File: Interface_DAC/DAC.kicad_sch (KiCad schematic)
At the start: 14 parts, among them U5 PCM1794A

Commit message: Footprint Arrangement
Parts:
- C43, C45, C47, C50: footprint (none) -> Capacitor_Tantalum_SMD:CP_EIA-2012-12_Kemet-R
- C44, C46, C48: footprint (none) -> Capacitor_SMD:C_0402_1005Metric
- C49: footprint (none) -> Capacitor_Tantalum_SMD:CP_EIA-3216-18_Kemet-A
- R11, R12, R4, R5, R8: footprint (none) -> Resistor_SMD:R_0402_1005Metric
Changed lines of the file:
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@@
 			)
 		)
-		(property "Footprint" ""
+		(property "Footprint" "Resistor_SMD:R_0402_1005Metric"
 			(at 69.85 112.268 90)
 			(effects
@@
 			)
 		)
-		(property "Footprint" ""
+		(property "Footprint" "Capacitor_Tantalum_SMD:CP_EIA-2012-12_Kemet-R"
 			(at 89.8652 69.85 0)
 			(effects
@@
 			)
 		)
-		(property "Footprint" ""
+		(property "Footprint" "Resistor_SMD:R_0402_1005Metric"
 			(at 49.53 117.348 90)
 			(effects
@@
 			)
 		)
-		(property "Footprint" ""
+		(property "Footprint" "Resistor_SMD:R_0402_1005Metric"
 			(at 59.69 114.808 90)
 			(effects
@@
 			)
 		)
-		(property "Footprint" ""
+		(property "Footprint" "Capacitor_Tantalum_SMD:CP_EIA-2012-12_Kemet-R"
 			(at 115.2652 62.23 0)
 			(effects
@@
 			)
 		)
-		(property "Footprint" ""
+		(property "Footprint" "Capacitor_SMD:C_0402_1005Metric"
 			(at 125.4252 62.23 0)
 			(effects
@@
 			)
 		)
-		(property "Footprint" ""
+		(property "Footprint" "Resistor_SMD:R_0402_1005Metric"
 			(at 80.01 109.728 90)
 			(effects
@@
 			)
 		)
-		(property "Footprint" ""
+		(property "Footprint" "Capacitor_Tantalum_SMD:CP_EIA-2012-12_Kemet-R"
 			(at 115.2652 85.09 0)
 			(effects
@@
 			)
 		)
-		(property "Footprint" ""
+		(property "Footprint" "Capacitor_Tantalum_SMD:CP_EIA-3216-18_Kemet-A"
 			(at 127.9652 105.41 0)
 			(effects
@@
 			)
 		)
-		(property "Footprint" ""
+		(property "Footprint" "Resistor_SMD:R_0402_1005Metric"
 			(at 128.27 140.208 90)
 			(effects
@@
 			)
 		)
-		(property "Footprint" ""
+		(property "Footprint" "Capacitor_SMD:C_0402_1005Metric"
 			(at 89.8652 90.17 0)
 			(effects
@@
 			)
 		)
-		(property "Footprint" ""
+		(property "Footprint" "Capacitor_SMD:C_0402_1005Metric"
 			(at 125.4252 85.09 0)
 			(effects
@@
 			)
 		)
-		(property "Footprint" ""
+		(property "Footprint" "Capacitor_Tantalum_SMD:CP_EIA-2012-12_Kemet-R"
 			(at 79.7052 90.17 0)
 			(effects

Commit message: Schematic Tinkering and PCB Layout
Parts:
- added C48: 10u, Capacitor_SMD:C_0402_1005Metric, symbol Device:C
- added R6: 47k, Resistor_SMD:R_0402_1005Metric, symbol Device:R
- C40: renamed from C45; footprint Capacitor_Tantalum_SMD:CP_EIA-2012-12_Kemet-R -> Capacitor_SMD:C_0402_1005Metric; symbol Device:C_Polarized -> Device:C
- C42: renamed from C50; footprint Capacitor_Tantalum_SMD:CP_EIA-2012-12_Kemet-R -> Capacitor_SMD:C_0402_1005Metric; symbol Device:C_Polarized -> Device:C
- C43: footprint Capacitor_Tantalum_SMD:CP_EIA-2012-12_Kemet-R -> Capacitor_SMD:C_0402_1005Metric; symbol Device:C_Polarized -> Device:C
- C45: renamed from C47; footprint Capacitor_Tantalum_SMD:CP_EIA-2012-12_Kemet-R -> Capacitor_SMD:C_0402_1005Metric; symbol Device:C_Polarized -> Device:C
- C47: renamed from C49; value 47u -> 10u; footprint Capacitor_Tantalum_SMD:CP_EIA-3216-18_Kemet-A -> Capacitor_SMD:C_0402_1005Metric; symbol Device:C_Polarized -> Device:C
- renumbered C46 to C41, C48 to C46, R5 to R2, R8 to R3, R11 to R4, R12 to R5, R4 to R7, U5 to U4
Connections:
- net +3.3V: now also R6.1
- net GND: now also U4.1 (MONO), U4.10 (MUTE), U4.11 (FMT0), U4.12 (FMT1), U4.2 (CHSL), U4.3 (DEM)
- net VBUS: now also C48.1
- net at C47.2, U4.22 (VCOML): no longer U4.21 (VCOMR)
- net at U4.14 (~{RST}): now also R6.2
- net SCK renamed I2S_SCK
- new net: C48.2, U4.21 (VCOMR)

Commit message: Schematic Tinkering and PCB Layout
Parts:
- added C40, C50, C53, C56: 4.7n, Capacitor_SMD:C_0402_1005Metric, symbol Device:C
- added C43, C49, C54, C55: 10n, Capacitor_SMD:C_0402_1005Metric, symbol Device:C
- added R13, R20, R3, R8: 820, Resistor_SMD:R_0402_1005Metric, symbol Device:R
- added R14, R19, R4, R7: 240, Resistor_SMD:R_0402_1005Metric, symbol Device:R
- added R17, R18, R5, R6: 510, Resistor_SMD:R_0402_1005Metric, symbol Device:R
- added U4, U6: OPA1612AxD, Package_SON:WSON-8-1EP_3x3mm_P0.5mm_EP1.2x2mm_ThermalVias, symbol Amplifier_Operational:OPA1612AxD
- added U5: OPA1612AxD, Package_SO:SOIC-8_3.9x4.9mm_P1.27mm, symbol Amplifier_Operational:OPA1612AxD
- renumbered C40 to C41, C41 to C42, C42 to C44, C43 to C45, C44 to C46, C45 to C47, C46 to C48, C47 to C51, C48 to C52, R3 to R10, R4 to R11, R5 to R12, R6 to R15, R7 to R16, R2 to R9, U4 to U7
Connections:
- net GND: now also C49.2, C55.2, R19.2, R7.2, U4.3 (+), U4.5 (+), U6.3 (+), U6.5 (+)
- net IOUTRP: now reaches U7.17 (IOUTR+)
- net IOUTRP: now also C53.1, R13.1, U6.6 (-)
- net IOUTRN: now reaches U7.18 (IOUTR-)
- net IOUTRN: now also C56.1, R20.1, U6.2 (-)
- net IOUTLP: now reaches U7.25 (IOUTL+)
- net IOUTLP: now also C40.1, R3.1, U4.6 (-)
- net IOUTLN: now reaches U7.26 (IOUTL-)
- net IOUTLN: now also C50.1, R8.1, U4.2 (-)
- new net: C53.2, R13.2, R17.1, U6.7
- new net: C54.1, R14.1, R17.2, U5.6 (-)
- new net: C50.2, R6.1, R8.2, U4.1
- new net: C56.2, R18.1, R20.2, U6.1
- new net: C55.1, R18.2, R19.1, U5.5 (+)
- new net: C43.1, R4.1, R5.2, U5.2 (-)
- new net: C49.1, R6.2, R7.1, U5.3 (+)
- new net: C40.2, R3.2, R5.1, U4.7
- new net +9VA: U4.8 (V+), U5.8 (V+), U6.8 (V+)
- new net -9VA: U4.4 (V-), U5.4 (V-), U6.4 (V-)
- new net LOUT: C43.2, R4.2, U5.1
- new net ROUT: C54.2, R14.2, U5.7
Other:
- moved on the sheet: C41, C42, C44, C45, C46, C47, C48, C51, C52, R10, R11, R12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

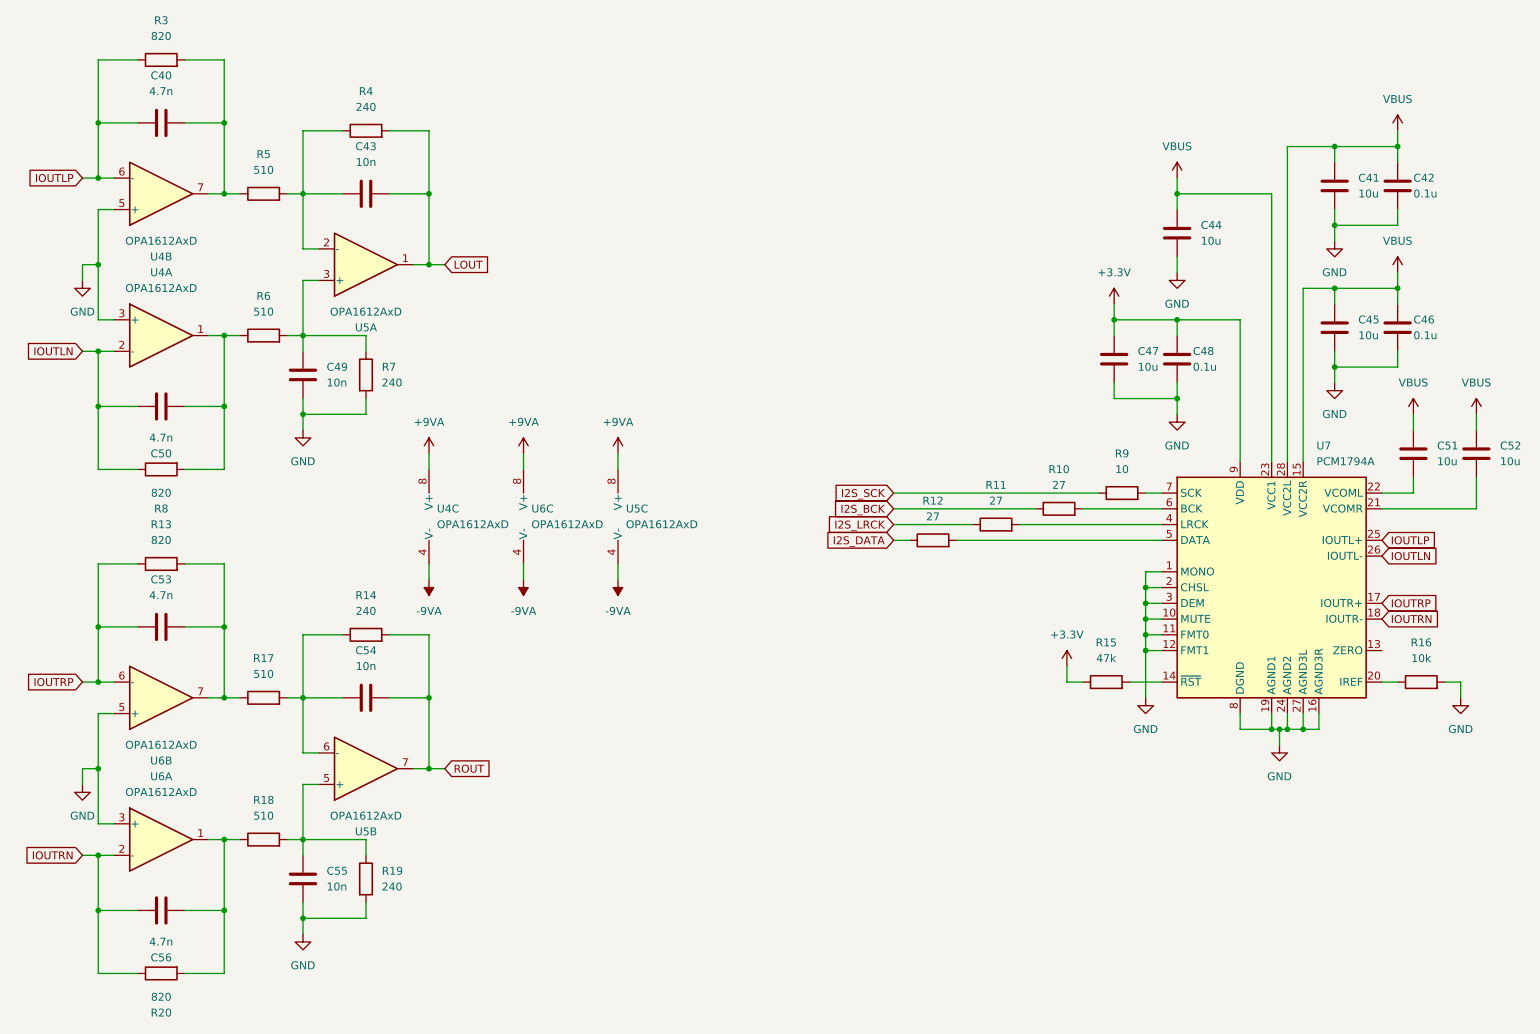
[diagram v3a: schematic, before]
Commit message: Schematic Design and Library Relink
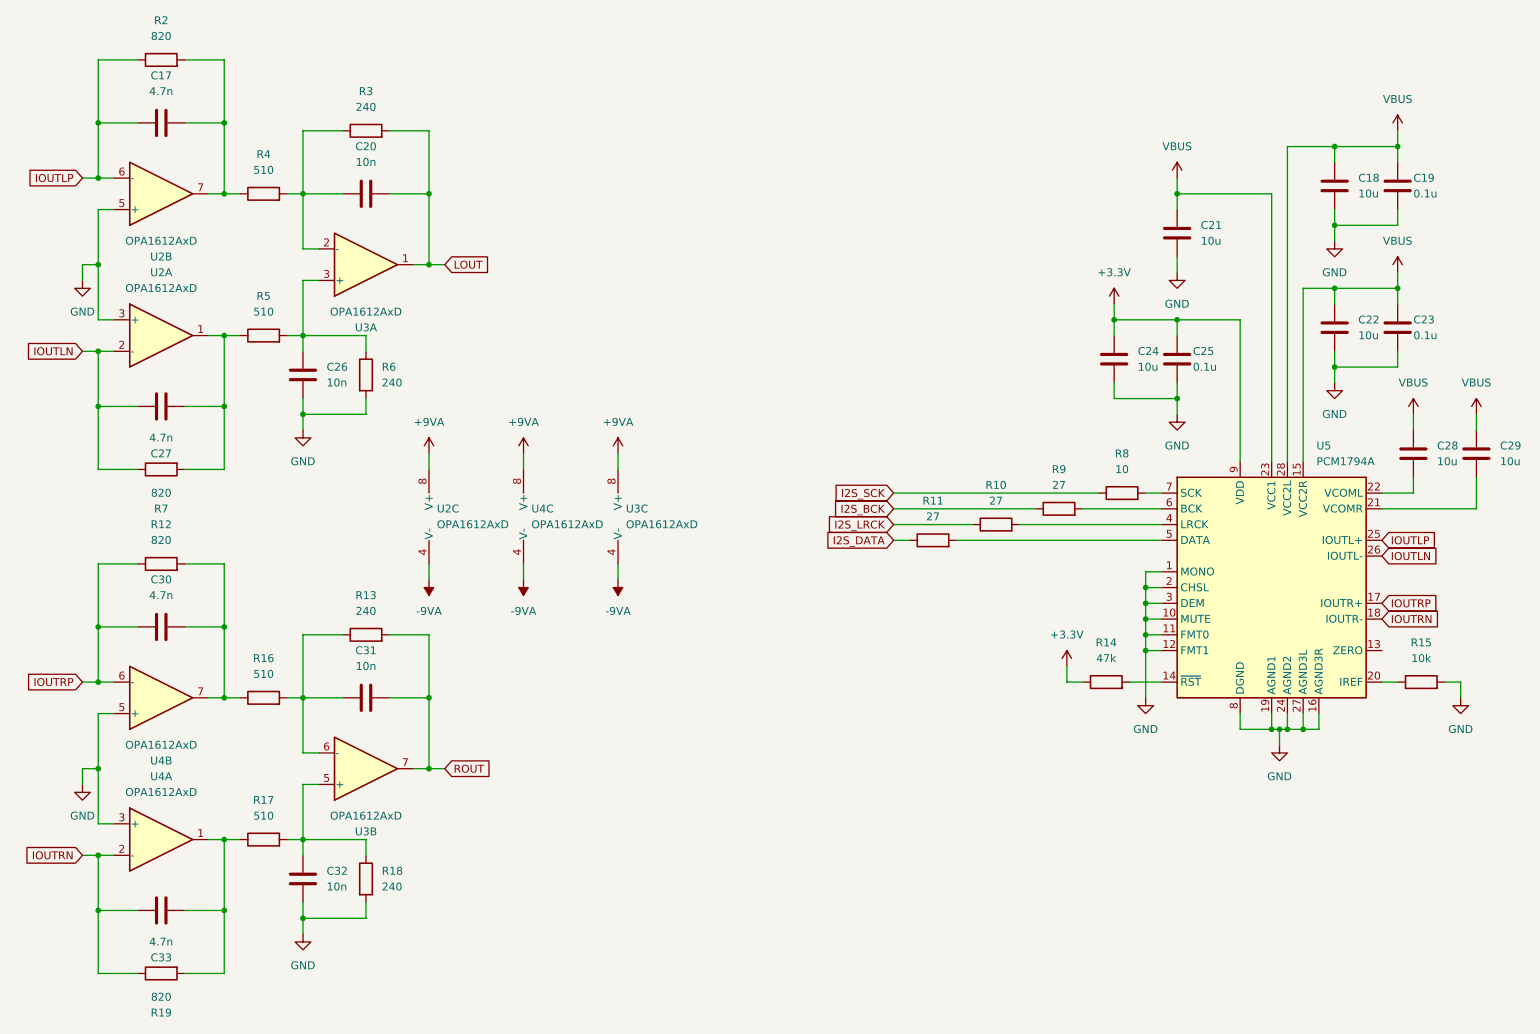
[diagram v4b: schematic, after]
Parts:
- renumbered C40 to C17, C41 to C18, C42 to C19, C43 to C20, C44 to C21, C45 to C22, C46 to C23, C47 to C24, C48 to C25, C49 to C26, C50 to C27, C51 to C28, C52 to C29, C53 to C30, C54 to C31, C55 to C32, C56 to C33, R11 to R10, R12 to R11, R13 to R12, R14 to R13, R15 to R14, R16 to R15, R17 to R16, R18 to R17, R19 to R18, R20 to R19, R3 to R2, R4 to R3, R5 to R4, R6 to R5, R7 to R6, R8 to R7, R9 to R8, R10 to R9, U4 to U2, U5 to U3, U6 to U4, U7 to U5

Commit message: Schematic Design
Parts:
- renumbered R9 to R10, R10 to R11, R11 to R12, R12 to R13, R13 to R14, R14 to R15, R15 to R16, R16 to R17, R17 to R18, R18 to R19, R19 to R20, R2 to R3, R3 to R4, R4 to R5, R5 to R6, R6 to R7, R7 to R8, R8 to R9
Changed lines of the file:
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@@
 		(dnp no)
 		(fields_autoplaced yes)
-		(property "Reference" "R16"
+		(property "Reference" "R17"
 			(at 66.04 125.73 90)
 			(effects
@@
 			(project "Interface_DAC"
 				(path "/0e211ec1-40f7-401e-8406-03ff71d7b636/4fe518ed-419a-404a-8437-744bb00d2e80"
-					(reference "R16")
+					(reference "R17")
 					(unit 1)
 				)
@@
 		(dnp no)
 		(fields_autoplaced yes)
-		(property "Reference" "R9"
+		(property "Reference" "R10"
 			(at 194.31 95.25 90)
 			(effects
@@
 			(project "Interface_DAC"
 				(path "/0e211ec1-40f7-401e-8406-03ff71d7b636/4fe518ed-419a-404a-8437-744bb00d2e80"
-					(reference "R9")
+					(reference "R10")
 					(unit 1)
 				)
@@
 		(dnp no)
 		(fields_autoplaced yes)
-		(property "Reference" "R11"
+		(property "Reference" "R12"
 			(at 173.99 100.33 90)
 			(effects
@@
 			(project "Interface_DAC"
 				(path "/0e211ec1-40f7-401e-8406-03ff71d7b636/4fe518ed-419a-404a-8437-744bb00d2e80"
-					(reference "R11")
+					(reference "R12")
 					(unit 1)
 				)
@@
 		(dnp no)
 		(fields_autoplaced yes)
-		(property "Reference" "R13"
+		(property "Reference" "R14"
 			(at 82.55 115.57 90)
 			(effects
@@
 			(project "Interface_DAC"
 				(path "/0e211ec1-40f7-401e-8406-03ff71d7b636/4fe518ed-419a-404a-8437-744bb00d2e80"
-					(reference "R13")
+					(reference "R14")
 					(unit 1)
 				)
@@
 		(dnp no)
 		(fields_autoplaced yes)
-		(property "Reference" "R17"
+		(property "Reference" "R18"
 			(at 66.04 148.59 90)
 			(effects
@@
 			(project "Interface_DAC"
 				(path "/0e211ec1-40f7-401e-8406-03ff71d7b636/4fe518ed-419a-404a-8437-744bb00d2e80"
-					(reference "R17")
+					(reference "R18")
 					(unit 1)
 				)
@@
 		(dnp no)
 		(fields_autoplaced yes)
-		(property "Reference" "R2"
+		(property "Reference" "R3"
 			(at 49.53 22.86 90)
 			(effects
@@
 			(project "Interface_DAC"
 				(path "/0e211ec1-40f7-401e-8406-03ff71d7b636/4fe518ed-419a-404a-8437-744bb00d2e80"
-					(reference "R2")
+					(reference "R3")
 					(unit 1)
 				)
@@
 		(dnp no)
 		(fields_autoplaced yes)
-		(property "Reference" "R12"
+		(property "Reference" "R13"
 			(at 49.53 104.14 90)
 			(effects
@@
 			(project "Interface_DAC"
 				(path "/0e211ec1-40f7-401e-8406-03ff71d7b636/4fe518ed-419a-404a-8437-744bb00d2e80"
-					(reference "R12")
+					(reference "R13")
 					(unit 1)
 				)
@@
 		(dnp no)
 		(fields_autoplaced yes)
-		(property "Reference" "R6"
+		(property "Reference" "R7"
 			(at 85.09 78.7399 0)
 			(effects
@@
 			(project "Interface_DAC"
 				(path "/0e211ec1-40f7-401e-8406-03ff71d7b636/4fe518ed-419a-404a-8437-744bb00d2e80"
-					(reference "R6")
+					(reference "R7")
 					(unit 1)
 				)
@@
 		(dnp no)
 		(fields_autoplaced yes)
-		(property "Reference" "R10"
+		(property "Reference" "R11"
 			(at 184.15 97.79 90)
 			(effects
@@
 			(project "Interface_DAC"
 				(path "/0e211ec1-40f7-401e-8406-03ff71d7b636/4fe518ed-419a-404a-8437-744bb00d2e80"
-					(reference "R10")
+					(reference "R11")
 					(unit 1)
 				)
@@
 		(dnp no)
 		(fields_autoplaced yes)
-		(property "Reference" "R4"
+		(property "Reference" "R5"
 			(at 66.04 44.45 90)
 			(effects
@@
 			(project "Interface_DAC"
 				(path "/0e211ec1-40f7-401e-8406-03ff71d7b636/4fe518ed-419a-404a-8437-744bb00d2e80"
-					(reference "R4")
+					(reference "R5")
 					(unit 1)
 				)
@@
 		(on_board yes)
 		(dnp no)
-		(property "Reference" "R7"
+		(property "Reference" "R8"
 			(at 49.53 101.6 90)
 			(effects
@@
 			(project "Interface_DAC"
 				(path "/0e211ec1-40f7-401e-8406-03ff71d7b636/4fe518ed-419a-404a-8437-744bb00d2e80"
-					(reference "R7")
+					(reference "R8")
 					(unit 1)
 				)
@@
 		(dnp no)
 		(fields_autoplaced yes)
-		(property "Reference" "R14"
+		(property "Reference" "R15"
 			(at 201.93 123.19 90)
 			(effects
@@
 			(project "Interface_DAC"
 				(path "/0e211ec1-40f7-401e-8406-03ff71d7b636/4fe518ed-419a-404a-8437-744bb00d2e80"
-					(reference "R14")
+					(reference "R15")
 					(unit 1)
 				)
@@
 		(dnp no)
 		(fields_autoplaced yes)
-		(property "Reference" "R3"
+		(property "Reference" "R4"
 			(at 82.55 34.29 90)
 			(effects
@@
 			(project "Interface_DAC"
 				(path "/0e211ec1-40f7-401e-8406-03ff71d7b636/4fe518ed-419a-404a-8437-744bb00d2e80"
-					(reference "R3")
+					(reference "R4")
 					(unit 1)
 				)
@@
 		(on_board yes)
 		(dnp no)
-		(property "Reference" "R19"
+		(property "Reference" "R20"
 			(at 49.53 182.88 90)
 			(effects
@@
 			(project "Interface_DAC"
 				(path "/0e211ec1-40f7-401e-8406-03ff71d7b636/4fe518ed-419a-404a-8437-744bb00d2e80"
-					(reference "R19")
+					(reference "R20")
 					(unit 1)
 				)
@@
 		(dnp no)
 		(fields_autoplaced yes)
-		(property "Reference" "R18"
+		(property "Reference" "R19"
 			(at 85.09 160.0199 0)
 			(effects
@@
 			(project "Interface_DAC"
 				(path "/0e211ec1-40f7-401e-8406-03ff71d7b636/4fe518ed-419a-404a-8437-744bb00d2e80"
-					(reference "R18")
+					(reference "R19")
 					(unit 1)
 				)
@@
 		(dnp no)
 		(fields_autoplaced yes)
-		(property "Reference" "R8"
+		(property "Reference" "R9"
 			(at 204.47 92.71 90)
 			(effects
@@
 			(project ""
 				(path "/0e211ec1-40f7-401e-8406-03ff71d7b636/4fe518ed-419a-404a-8437-744bb00d2e80"
-					(reference "R8")
+					(reference "R9")
 					(unit 1)
 				)
@@
 		(dnp no)
 		(fields_autoplaced yes)
-		(property "Reference" "R15"
+		(property "Reference" "R16"
 			(at 252.73 123.19 90)
 			(effects
@@
 			(project ""
 				(path "/0e211ec1-40f7-401e-8406-03ff71d7b636/4fe518ed-419a-404a-8437-744bb00d2e80"
-					(reference "R15")
+					(reference "R16")
 					(unit 1)
 				)
@@
 		(dnp no)
 		(fields_autoplaced yes)
-		(property "Reference" "R5"
+		(property "Reference" "R6"
 			(at 66.04 67.31 90)
 			(effects
@@
 			(project "Interface_DAC"
 				(path "/0e211ec1-40f7-401e-8406-03ff71d7b636/4fe518ed-419a-404a-8437-744bb00d2e80"
-					(reference "R5")
+					(reference "R6")
 					(unit 1)
 				)
